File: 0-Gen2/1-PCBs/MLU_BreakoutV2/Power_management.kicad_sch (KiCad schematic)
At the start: 9 parts, among them J6 430450228, SW1 09.03201.02, U1 BA033CC0FP-E2

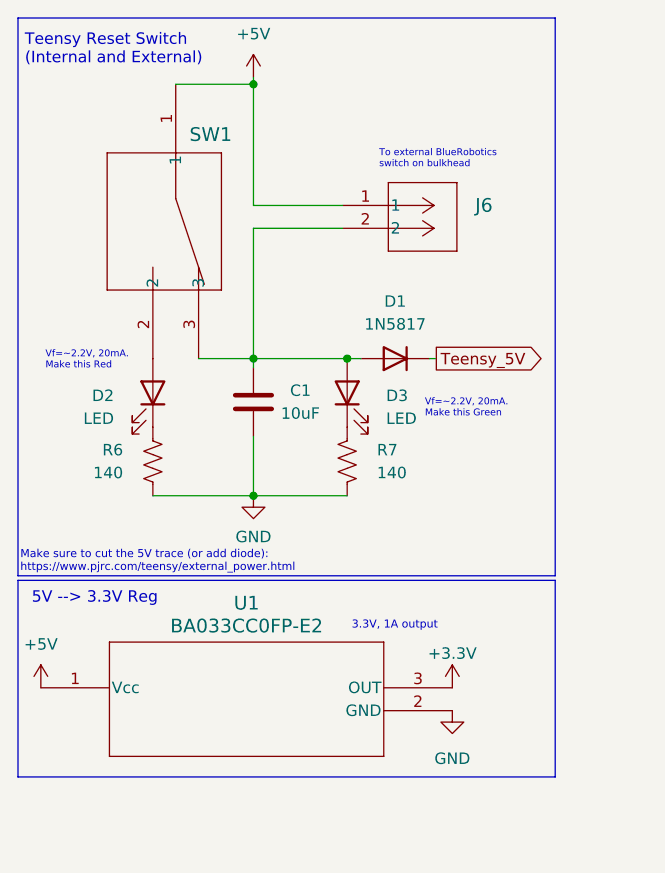
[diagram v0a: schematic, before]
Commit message: [add] major layout updates
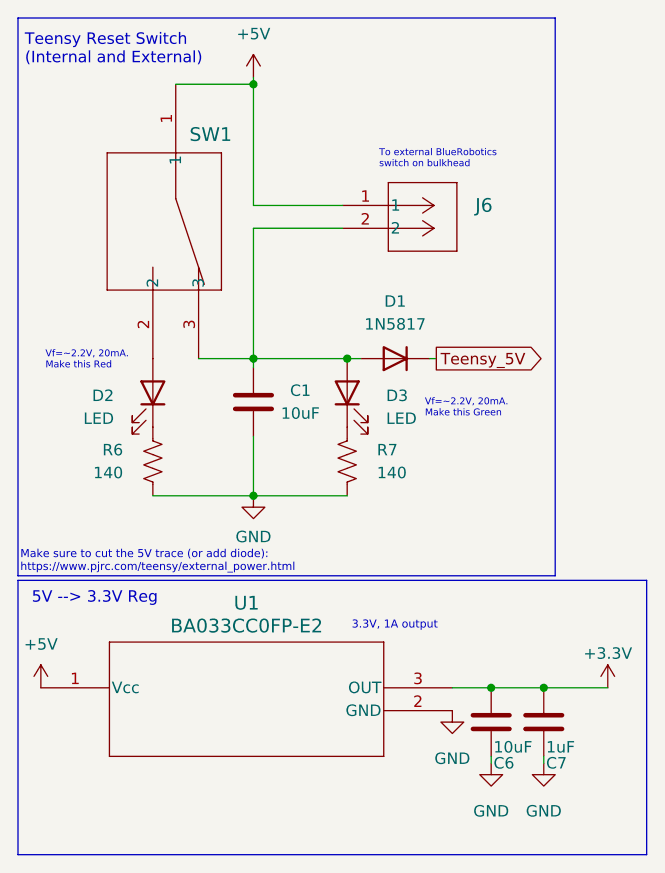
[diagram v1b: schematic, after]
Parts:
- added C6: 10uF, Capacitor_SMD:C_0805_2012Metric_Pad1.18x1.45mm_HandSolder, symbol Device:C
- added C7: 1uF, Capacitor_SMD:C_0805_2012Metric_Pad1.18x1.45mm_HandSolder, symbol Device:C
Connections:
- net +3.3V: now also C6.1, C7.1
- net GND: now also C6.2, C7.2

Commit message: before restructure
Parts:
- renumbered C1 to C5, J6 to J25, R6 to R8, R7 to R9, U1 to U6
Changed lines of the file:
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@@
 		(dnp no)
 		(fields_autoplaced yes)
-		(property "Reference" "#PWR024"
+		(property "Reference" "#PWR0147"
 			(at 143.002 64.008 0)
 			(effects
@@
 			(project "MLU_BreakoutV2"
 				(path "/55121ba7-5d22-4fe3-93aa-7f76d75b410c/9e78e214-9eaa-4133-a14f-75961ce763bc"
-					(reference "#PWR024")
+					(reference "#PWR0147")
 					(unit 1)
 				)
@@
 		(dnp no)
 		(fields_autoplaced yes)
-		(property "Reference" "#PWR053"
+		(property "Reference" "#PWR0152"
 			(at 169.418 142.748 0)
 			(effects
@@
 			(project "MLU_BreakoutV2"
 				(path "/55121ba7-5d22-4fe3-93aa-7f76d75b410c/9e78e214-9eaa-4133-a14f-75961ce763bc"
-					(reference "#PWR053")
+					(reference "#PWR0152")
 					(unit 1)
 				)
@@
 		(dnp no)
 		(fields_autoplaced yes)
-		(property "Reference" "#PWR042"
+		(property "Reference" "#PWR0149"
 			(at 119.38 131.826 0)
 			(effects
@@
 			(project "MLU_BreakoutV2"
 				(path "/55121ba7-5d22-4fe3-93aa-7f76d75b410c/9e78e214-9eaa-4133-a14f-75961ce763bc"
-					(reference "#PWR042")
+					(reference "#PWR0149")
 					(unit 1)
 				)
@@
 		(dnp no)
 		(fields_autoplaced yes)
-		(property "Reference" "#PWR044"
+		(property "Reference" "#PWR0151"
 			(at 165.1 136.906 0)
 			(effects
@@
 			(project "MLU_BreakoutV2"
 				(path "/55121ba7-5d22-4fe3-93aa-7f76d75b410c/9e78e214-9eaa-4133-a14f-75961ce763bc"
-					(reference "#PWR044")
+					(reference "#PWR0151")
 					(unit 1)
 				)
@@
 		(dnp no)
 		(fields_autoplaced yes)
-		(property "Reference" "J6"
+		(property "Reference" "J25"
 			(at 167.64 74.4219 0)
 			(effects
@@
 			(project "MLU_BreakoutV2"
 				(path "/55121ba7-5d22-4fe3-93aa-7f76d75b410c/9e78e214-9eaa-4133-a14f-75961ce763bc"
-					(reference "J6")
+					(reference "J25")
 					(unit 1)
 				)
@@
 		(on_board yes)
 		(dnp no)
-		(property "Reference" "R7"
+		(property "Reference" "R9"
 			(at 156.718 101.5999 0)
 			(effects
@@
 			(project "MLU_BreakoutV2"
 				(path "/55121ba7-5d22-4fe3-93aa-7f76d75b410c/9e78e214-9eaa-4133-a14f-75961ce763bc"
-					(reference "R7")
+					(reference "R9")
 					(unit 1)
 				)
@@
 		(dnp no)
 		(fields_autoplaced yes)
-		(property "Reference" "U1"
+		(property "Reference" "U6"
 			(at 142.24 118.618 0)
 			(effects
@@
 			(project "MLU_BreakoutV2"
 				(path "/55121ba7-5d22-4fe3-93aa-7f76d75b410c/9e78e214-9eaa-4133-a14f-75961ce763bc"
-					(reference "U1")
+					(reference "U6")
 					(unit 1)
 				)
@@
 		(dnp no)
 		(fields_autoplaced yes)
-		(property "Reference" "#PWR054"
+		(property "Reference" "#PWR0153"
 			(at 175.26 142.748 0)
 			(effects
@@
 			(project "MLU_BreakoutV2"
 				(path "/55121ba7-5d22-4fe3-93aa-7f76d75b410c/9e78e214-9eaa-4133-a14f-75961ce763bc"
-					(reference "#PWR054")
+					(reference "#PWR0153")
 					(unit 1)
 				)
@@
 		(dnp no)
 		(fields_autoplaced yes)
-		(property "Reference" "#PWR037"
+		(property "Reference" "#PWR0148"
 			(at 143.002 113.03 0)
 			(effects
@@
 			(project "MLU_BreakoutV2"
 				(path "/55121ba7-5d22-4fe3-93aa-7f76d75b410c/9e78e214-9eaa-4133-a14f-75961ce763bc"
-					(reference "#PWR037")
+					(reference "#PWR0148")
 					(unit 1)
 				)
@@
 		(on_board yes)
 		(dnp no)
-		(property "Reference" "R6"
+		(property "Reference" "R8"
 			(at 128.524 101.5999 0)
 			(effects
@@
 			(project "MLU_BreakoutV2"
 				(path "/55121ba7-5d22-4fe3-93aa-7f76d75b410c/9e78e214-9eaa-4133-a14f-75961ce763bc"
-					(reference "R6")
+					(reference "R8")
 					(unit 1)
 				)
@@
 		(on_board yes)
 		(dnp no)
-		(property "Reference" "C1"
+		(property "Reference" "C5"
 			(at 147.066 94.9959 0)
 			(effects
@@
 			(project "MLU_BreakoutV2"
 				(path "/55121ba7-5d22-4fe3-93aa-7f76d75b410c/9e78e214-9eaa-4133-a14f-75961ce763bc"
-					(reference "C1")
+					(reference "C5")
 					(unit 1)
 				)
@@
 		(on_board yes)
 		(dnp no)
-		(property "Reference" "#PWR043"
+		(property "Reference" "#PWR0150"
 			(at 182.372 131.826 0)
 			(effects
@@
 			(project "MLU_BreakoutV2"
 				(path "/55121ba7-5d22-4fe3-93aa-7f76d75b410c/9e78e214-9eaa-4133-a14f-75961ce763bc"
-					(reference "#PWR043")
+					(reference "#PWR0150")
 					(unit 1)
 				)

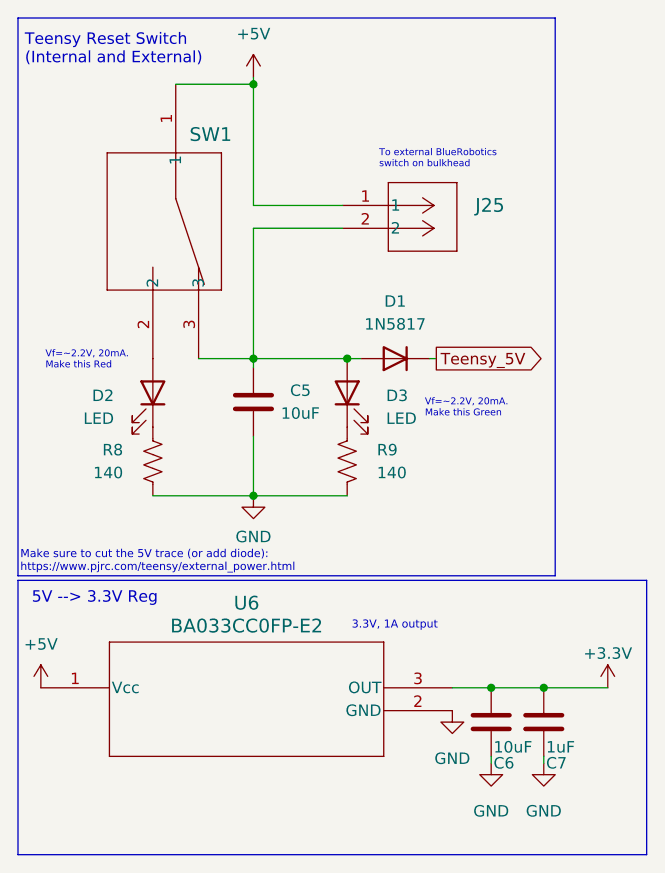
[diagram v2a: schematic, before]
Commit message: [bugfix] rescued footprints
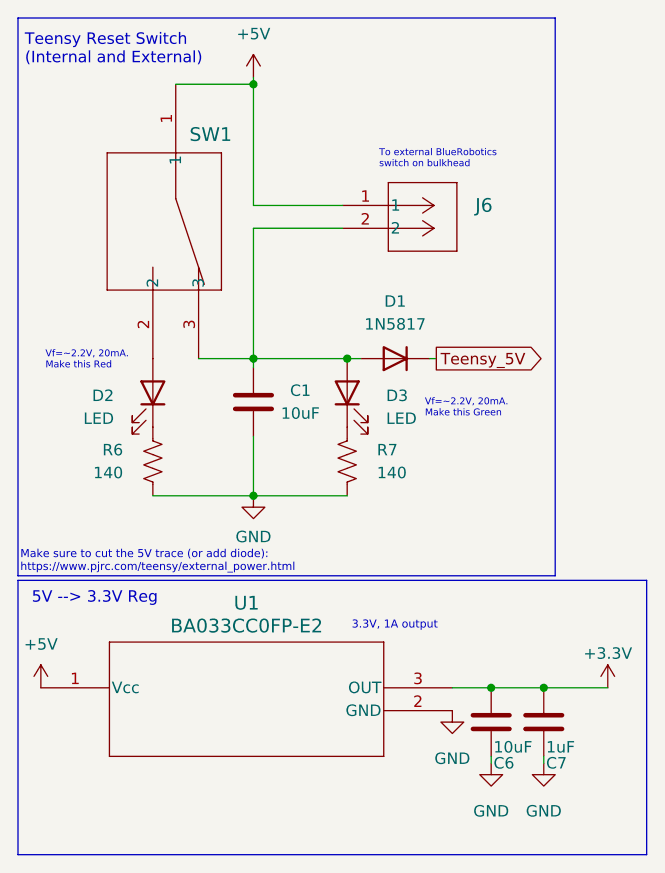
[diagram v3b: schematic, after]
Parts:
- renumbered C5 to C1, J25 to J6, R8 to R6, R9 to R7, U6 to U1
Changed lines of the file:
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@@
 		(dnp no)
 		(fields_autoplaced yes)
-		(property "Reference" "#PWR0147"
+		(property "Reference" "#PWR024"
 			(at 143.002 64.008 0)
 			(effects
@@
 			(project "MLU_BreakoutV2"
 				(path "/55121ba7-5d22-4fe3-93aa-7f76d75b410c/9e78e214-9eaa-4133-a14f-75961ce763bc"
-					(reference "#PWR0147")
+					(reference "#PWR024")
 					(unit 1)
 				)
@@
 		(dnp no)
 		(fields_autoplaced yes)
-		(property "Reference" "#PWR0152"
+		(property "Reference" "#PWR053"
 			(at 169.418 142.748 0)
 			(effects
@@
 			(project "MLU_BreakoutV2"
 				(path "/55121ba7-5d22-4fe3-93aa-7f76d75b410c/9e78e214-9eaa-4133-a14f-75961ce763bc"
-					(reference "#PWR0152")
+					(reference "#PWR053")
 					(unit 1)
 				)
@@
 		(dnp no)
 		(fields_autoplaced yes)
-		(property "Reference" "#PWR0149"
+		(property "Reference" "#PWR042"
 			(at 119.38 131.826 0)
 			(effects
@@
 			(project "MLU_BreakoutV2"
 				(path "/55121ba7-5d22-4fe3-93aa-7f76d75b410c/9e78e214-9eaa-4133-a14f-75961ce763bc"
-					(reference "#PWR0149")
+					(reference "#PWR042")
 					(unit 1)
 				)
@@
 		(dnp no)
 		(fields_autoplaced yes)
-		(property "Reference" "#PWR0151"
+		(property "Reference" "#PWR044"
 			(at 165.1 136.906 0)
 			(effects
@@
 			(project "MLU_BreakoutV2"
 				(path "/55121ba7-5d22-4fe3-93aa-7f76d75b410c/9e78e214-9eaa-4133-a14f-75961ce763bc"
-					(reference "#PWR0151")
+					(reference "#PWR044")
 					(unit 1)
 				)
@@
 		(dnp no)
 		(fields_autoplaced yes)
-		(property "Reference" "J25"
+		(property "Reference" "J6"
 			(at 167.64 74.4219 0)
 			(effects
@@
 			(project "MLU_BreakoutV2"
 				(path "/55121ba7-5d22-4fe3-93aa-7f76d75b410c/9e78e214-9eaa-4133-a14f-75961ce763bc"
-					(reference "J25")
+					(reference "J6")
 					(unit 1)
 				)
@@
 		(on_board yes)
 		(dnp no)
-		(property "Reference" "R9"
+		(property "Reference" "R7"
 			(at 156.718 101.5999 0)
 			(effects
@@
 			(project "MLU_BreakoutV2"
 				(path "/55121ba7-5d22-4fe3-93aa-7f76d75b410c/9e78e214-9eaa-4133-a14f-75961ce763bc"
-					(reference "R9")
+					(reference "R7")
 					(unit 1)
 				)
@@
 		(dnp no)
 		(fields_autoplaced yes)
-		(property "Reference" "U6"
+		(property "Reference" "U1"
 			(at 142.24 118.618 0)
 			(effects
@@
 			(project "MLU_BreakoutV2"
 				(path "/55121ba7-5d22-4fe3-93aa-7f76d75b410c/9e78e214-9eaa-4133-a14f-75961ce763bc"
-					(reference "U6")
+					(reference "U1")
 					(unit 1)
 				)
@@
 		(dnp no)
 		(fields_autoplaced yes)
-		(property "Reference" "#PWR0153"
+		(property "Reference" "#PWR054"
 			(at 175.26 142.748 0)
 			(effects
@@
 			(project "MLU_BreakoutV2"
 				(path "/55121ba7-5d22-4fe3-93aa-7f76d75b410c/9e78e214-9eaa-4133-a14f-75961ce763bc"
-					(reference "#PWR0153")
+					(reference "#PWR054")
 					(unit 1)
 				)
@@
 		(dnp no)
 		(fields_autoplaced yes)
-		(property "Reference" "#PWR0148"
+		(property "Reference" "#PWR037"
 			(at 143.002 113.03 0)
 			(effects
@@
 			(project "MLU_BreakoutV2"
 				(path "/55121ba7-5d22-4fe3-93aa-7f76d75b410c/9e78e214-9eaa-4133-a14f-75961ce763bc"
-					(reference "#PWR0148")
+					(reference "#PWR037")
 					(unit 1)
 				)
@@
 		(on_board yes)
 		(dnp no)
-		(property "Reference" "R8"
+		(property "Reference" "R6"
 			(at 128.524 101.5999 0)
 			(effects
@@
 			(project "MLU_BreakoutV2"
 				(path "/55121ba7-5d22-4fe3-93aa-7f76d75b410c/9e78e214-9eaa-4133-a14f-75961ce763bc"
-					(reference "R8")
+					(reference "R6")
 					(unit 1)
 				)
@@
 		(on_board yes)
 		(dnp no)
-		(property "Reference" "C5"
+		(property "Reference" "C1"
 			(at 147.066 94.9959 0)
 			(effects
@@
 			(project "MLU_BreakoutV2"
 				(path "/55121ba7-5d22-4fe3-93aa-7f76d75b410c/9e78e214-9eaa-4133-a14f-75961ce763bc"
-					(reference "C5")
+					(reference "C1")
 					(unit 1)
 				)
@@
 		(on_board yes)
 		(dnp no)
-		(property "Reference" "#PWR0150"
+		(property "Reference" "#PWR043"
 			(at 182.372 131.826 0)
 			(effects
@@
 			(project "MLU_BreakoutV2"
 				(path "/55121ba7-5d22-4fe3-93aa-7f76d75b410c/9e78e214-9eaa-4133-a14f-75961ce763bc"
-					(reference "#PWR0150")
+					(reference "#PWR043")
 					(unit 1)
 				)
